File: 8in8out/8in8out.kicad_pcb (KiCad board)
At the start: 2 copper layers, 100.1 x 86.4 mm, 62 parts, among them IC1 ATTINY48-A, J1 RJ45, J2 RJ45, J3 CONN_6, K110 G5T-1-12VDC, K120 G5T-1-12VDC, K130 G5T-1-12VDC, K140 G5T-1-12VDC, K150 G5T-1-12VDC, K160 G5T-1-12VDC, K170 G5T-1-12VDC, K180 G5T-1-12VDC, P1 CONN_5, P100 CONN_2, P101 CONN_2, P102 CONN_2, P103 CONN_2, P105 CONN_2, P106 CONN_2, P110 CONN_2, P120 CONN_2, P130 CONN_2, P140 CONN_2, P150 CONN_2, P160 CONN_2, P170 CONN_2, P180 CONN_2, P2 CONN_5, P3 CONN_10X2, P4 CONN_2, U1 7805, U10 OPTO-TRANSISTOR, U2 ULN2803, U20 OPTO-TRANSISTOR, U30 OPTO-TRANSISTOR, U40 OPTO-TRANSISTOR, U50 OPTO-TRANSISTOR, U60 OPTO-TRANSISTOR, U70 OPTO-TRANSISTOR, U80 OPTO-TRANSISTOR

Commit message: Serigraphie
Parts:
- moved R2 1.78 mm to (269.2, 115.6)
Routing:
- net +12V: track 172.0 -> 173.9 mm
- net N-0000088: track 3.14 -> 4.92 mm
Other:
- board text added: "0 1 2 3"
- board text added: "1"
- board text added: "12V"
- board text added: "12V-GND"
- board text added: "2"
- board text added: "3"
- board text added: "4"
- board text added: "5"
- board text added: "5V"
- board text added: "6"
- board text added: "7"
- board text added: "COM0"
- board text added: "COM1"
- board text added: "FRONT PANEL"
- board text added: "I2C"
- board text added: "I2C PORT"
- board text added: "IN 0"
- board text added: "ISP"
- board text added: "OUT 0"
- board text added: "OUT 1"
- board text added: "OUT 2"
- board text added: "OUT 3"
- board text added: "OUT 4"
- board text added: "OUT 5"
- board text added: "OUT 6"
- board text added: "OUT 7"
- board text added: "STATUS"
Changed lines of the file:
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@@
   (general
     (links 165)
-    (no_connects 14)
+    (no_connects 0)
     (area 180.235859 62.534801 283.060141 169.3672)
     (thickness 1.6002)
-    (drawings 28)
+    (drawings 58)
     (tracks 718)
     (zones 0)
@@
   )
   (layers
-    (15 Dessus signal)
-    (0 Dessous signal)
+    (15 Dessus signal hide)
+    (0 Dessous signal hide)
     (16 B.Adhes user)
     (17 F.Adhes user)
@@
     (23 F.Mask user)
     (24 Dwgs.User user)
-    (25 Cmts.User user)
+    (25 Cmts.User user hide)
     (26 Eco1.User user)
     (27 Eco2.User user)
@@
     (pad_to_mask_clearance 0.254)
     (aux_axis_origin 12.7 12.7)
-    (visible_elements 7FFE7DCF)
+    (visible_elements 7FFF7FFF)
     (pcbplotparams
       (layerselection 15761409)
@@
     (descr "Double rangee de contacts 2 x 12 pins")
     (tags CONN)
-    (fp_text reference P3 (at 0 -3.81) (layer F.SilkS)
+    (fp_text reference P3 (at 1.905 4.064) (layer F.SilkS)
       (effects (font (size 1.016 1.016) (thickness 0.27432)))
     )
@@
     (descr "Connecteurs 2 pins")
     (tags "CONN DEV")
-    (fp_text reference P100 (at 4.318 0.127 90) (layer F.SilkS)
+    (fp_text reference P100 (at 8.128 0.127 90) (layer F.SilkS)
       (effects (font (size 0.762 0.762) (thickness 0.1524)))
     )
@@
     (descr "Connecteurs 2 pins")
     (tags "CONN DEV")
-    (fp_text reference P101 (at 4.318 0.127 90) (layer F.SilkS)
+    (fp_text reference P101 (at 8.128 0.127 90) (layer F.SilkS)
       (effects (font (size 0.762 0.762) (thickness 0.1524)))
     )
@@
     (descr "Connecteurs 2 pins")
     (tags "CONN DEV")
-    (fp_text reference P103 (at 4.318 -0.127 90) (layer F.SilkS)
+    (fp_text reference P103 (at 8.128 -0.127 90) (layer F.SilkS)
       (effects (font (size 0.762 0.762) (thickness 0.1524)))
     )
@@
     (descr "Connecteurs 2 pins")
     (tags "CONN DEV")
-    (fp_text reference P102 (at 4.318 0.127 90) (layer F.SilkS)
+    (fp_text reference P102 (at 8.128 0.127 90) (layer F.SilkS)
       (effects (font (size 0.762 0.762) (thickness 0.1524)))
     )
@@
     (at 215.9 143.51)
     (attr smd)
-    (fp_text reference R51 (at 0 2.032) (layer F.SilkS)
+    (fp_text reference R51 (at 3.556 0 90) (layer F.SilkS)
       (effects (font (size 0.762 0.762) (thickness 0.127)))
     )
@@
   )
   (module SM1206 (layer Dessus)
-    (at 271.018 115.57 270)
+    (at 269.24 115.57 270)
     (attr smd)
     (fp_text reference R2 (at -3.556 0 360) (layer F.SilkS)
@@
     (at 199.39 143.51)
     (attr smd)
-    (fp_text reference R31 (at -1.524 2.286) (layer F.SilkS)
+    (fp_text reference R31 (at 3.556 0 90) (layer F.SilkS)
       (effects (font (size 0.762 0.762) (thickness 0.127)))
     )
@@
     (at 191.135 143.51)
     (attr smd)
-    (fp_text reference R21 (at -0.127 2.286) (layer F.SilkS)
+    (fp_text reference R21 (at 3.429 0 90) (layer F.SilkS)
       (effects (font (size 0.762 0.762) (thickness 0.127)))
     )
@@
     (at 207.518 143.51)
     (attr smd)
-    (fp_text reference R41 (at 0 2.032) (layer F.SilkS)
+    (fp_text reference R41 (at 3.556 0 90) (layer F.SilkS)
       (effects (font (size 0.762 0.762) (thickness 0.127)))
     )
@@
     (at 223.774 143.51)
     (attr smd)
-    (fp_text reference R61 (at 0 2.032) (layer F.SilkS)
+    (fp_text reference R61 (at 0 0 90) (layer F.SilkS)
       (effects (font (size 0.762 0.762) (thickness 0.127)))
     )
@@
     (at 229.235 143.51 180)
     (attr smd)
-    (fp_text reference R71 (at 1.397 -2.032 180) (layer F.SilkS)
+    (fp_text reference R71 (at -1.905 -2.032 180) (layer F.SilkS)
       (effects (font (size 0.762 0.762) (thickness 0.127)))
     )
@@
     (descr "Regulateur TO220 serie LM78xx")
     (tags "TR TO220")
-    (fp_text reference U1 (at -3.175 0 180) (layer F.SilkS)
+    (fp_text reference U1 (at -3.302 -4.318 180) (layer F.SilkS)
       (effects (font (size 1.524 1.016) (thickness 0.2032)))
     )
@@
     )
   )
+  (gr_text 12V-GND (at 241.554 146.304) (layer F.SilkS)
+    (effects (font (size 1.6 1.5) (thickness 0.3)))
+  )
+  (gr_text "I2C PORT" (at 255.27 138.176) (layer F.SilkS)
+    (effects (font (size 1.8 1.5) (thickness 0.3)))
+  )
+  (gr_line (start 226.568 116.84) (end 226.568 117.856) (angle 90) (layer F.SilkS) (width 0.381))
+  (gr_line (start 224.79 116.84) (end 226.568 116.84) (angle 90) (layer F.SilkS) (width 0.381))
+  (gr_line (start 224.79 117.856) (end 224.79 116.84) (angle 90) (layer F.SilkS) (width 0.381))
+  (gr_text ISP (at 226.06 115.062) (layer F.SilkS)
+    (effects (font (size 1.8 1.5) (thickness 0.3)))
+  )
+  (gr_text "FRONT PANEL" (at 207.518 116.332) (layer F.SilkS)
+    (effects (font (size 1.8 1.5) (thickness 0.3)))
+  )
+  (gr_text 12V (at 271.78 115.316 90) (layer F.SilkS)
+    (effects (font (size 1.6 1.5) (thickness 0.3)))
+  )
+  (gr_text 5V (at 279.146 115.51 90) (layer F.SilkS)
+    (effects (font (size 1.6 1.5) (thickness 0.3)))
+  )
+  (gr_text STATUS (at 260.604 114.554 90) (layer F.SilkS)
+    (effects (font (size 1.8 1.5) (thickness 0.3)))
+  )
+  (gr_text I2C (at 257.556 128.27) (layer F.SilkS)
+    (effects (font (size 1.8 1.5) (thickness 0.3)))
+  )
+  (gr_text "0 1 2 3" (at 250.19 122.682) (layer F.SilkS)
+    (effects (font (size 1.8 1.5) (thickness 0.3)))
+  )
+  (gr_text "OUT 7" (at 275.082 83.82) (layer F.SilkS)
+    (effects (font (thickness 0.3048)))
+  )
+  (gr_text "OUT 6" (at 262.89 83.82) (layer F.SilkS)
+    (effects (font (thickness 0.3048)))
+  )
+  (gr_text "OUT 5" (at 250.952 83.82) (layer F.SilkS)
+    (effects (font (thickness 0.3048)))
+  )
+  (gr_text "OUT 4" (at 238.506 83.82) (layer F.SilkS)
+    (effects (font (thickness 0.3048)))
+  )
+  (gr_text "OUT 3" (at 224.282 83.82) (layer F.SilkS)
+    (effects (font (thickness 0.3048)))
+  )
+  (gr_text "OUT 2" (at 212.344 83.82) (layer F.SilkS)
+    (effects (font (thickness 0.3048)))
+  )
+  (gr_text "OUT 1" (at 199.898 83.82) (layer F.SilkS)
+    (effects (font (thickness 0.3048)))
+  )
+  (gr_text "OUT 0" (at 187.96 83.82) (layer F.SilkS)
+    (effects (font (thickness 0.3048)))
+  )
+  (gr_text COM1 (at 224.79 146.558) (layer F.SilkS)
+    (effects (font (thickness 0.3048)))
+  )
+  (gr_text 7 (at 219.71 146.558) (layer F.SilkS)
+    (effects (font (thickness 0.3048)))
+  )
+  (gr_text 6 (at 215.9 146.558) (layer F.SilkS)
+    (effects (font (thickness 0.3048)))
+  )
+  (gr_text 5 (at 212.09 146.558) (layer F.SilkS)
+    (effects (font (thickness 0.3048)))
+  )
+  (gr_text 4 (at 208.28 146.558) (layer F.SilkS)
+    (effects (font (thickness 0.3048)))
+  )
+  (gr_text COM0 (at 202.946 146.558) (layer F.SilkS)
+    (effects (font (thickness 0.3048)))
+  )
+  (gr_text 3 (at 198.12 146.558) (layer F.SilkS)
+    (effects (font (thickness 0.3048)))
+  )
+  (gr_text 2 (at 194.31 146.558) (layer F.SilkS)
+    (effects (font (thickness 0.3048)))
+  )
+  (gr_text 1 (at 190.5 146.558) (layer F.SilkS)
+    (effects (font (thickness 0.3048)))
+  )
+  (gr_text "IN 0" (at 184.912 146.558) (layer F.SilkS)
+    (effects (font (thickness 0.3048)))
+  )
   (gr_line (start 208.661 122.936) (end 208.788 122.936) (angle 90) (layer F.SilkS) (width 0.381))
   (gr_line (start 208.661 124.587) (end 208.661 122.936) (angle 90) (layer F.SilkS) (width 0.381))
@@
   (gr_line (start 281.686 157.48) (end 281.686 71.12) (angle 90) (layer Edge.Cuts) (width 0.381))
   (gr_line (start 181.61 157.48) (end 181.61 71.12) (angle 90) (layer Edge.Cuts) (width 0.381))
+  (segment (start 274.828 110.617) (end 271.145 110.617) (width 0.50038) (layer Dessus) (net 1))
+  (segment (start 269.24 112.522) (end 269.24 113.919) (width 0.50038) (layer Dessus) (net 1))
+  (segment (start 271.145 110.617) (end 269.24 112.522) (width 0.50038) (layer Dessus) (net 1))
   (segment (start 239.649 149.733) (end 239.649 147.701) (width 0.50038) (layer Dessus) (net 1))
   (segment (start 239.649 147.701) (end 245.872 141.478) (width 0.50038) (layer Dessus) (net 1))
@@
   (segment (start 237.49 105.63098) (end 237.49 105.41) (width 0.50038) (layer Dessous) (net 1))
   (segment (start 237.49 105.41) (end 237.49 105.63098) (width 0.50038) (layer Dessous) (net 1))
-  (segment (start 271.018 113.919) (end 271.018 112.776) (width 0.50038) (layer Dessus) (net 1))
-  (segment (start 273.177 110.617) (end 274.828 110.617) (width 0.50038) (layer Dessus) (net 1))
-  (segment (start 271.018 112.776) (end 273.177 110.617) (width 0.50038) (layer Dessus) (net 1))
   (segment (start 255.778 107.823) (end 255.778 108.458) (width 0.50038) (layer Dessous) (net 1))
   (segment (start 255.778 108.458) (end 255.778 110.236) (width 0.50038) (layer Dessous) (net 1))
@@
   (segment (start 189.484 143.51) (end 189.484 139.954) (width 0.254) (layer Dessus) (net 54))
   (segment (start 197.739 143.51) (end 197.739 139.954) (width 0.254) (layer Dessus) (net 55))
-  (segment (start 271.018 117.221) (end 273.83486 117.221) (width 0.254) (layer Dessus) (net 56))
+  (segment (start 269.24 117.221) (end 273.83486 117.221) (width 0.254) (layer Dessus) (net 56))
   (segment (start 273.83486 117.221) (end 274.066 116.98986) (width 0.254) (layer Dessus) (net 56))
   (segment (start 278.384 120.269) (end 278.384 119.02186) (width 0.254) (layer Dessus) (net 57))

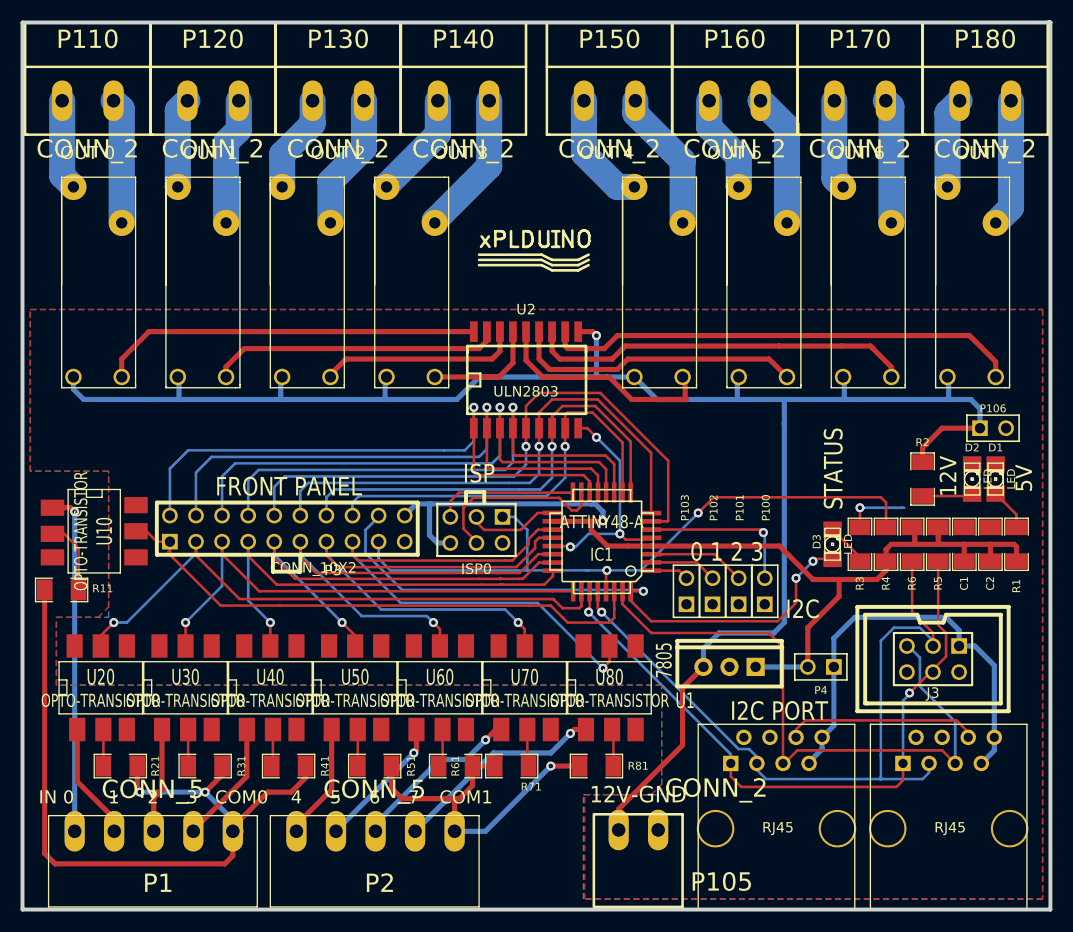
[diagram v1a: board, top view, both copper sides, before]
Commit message: Deplacement optos et r?sistances cause conflit boitier Serigraphie
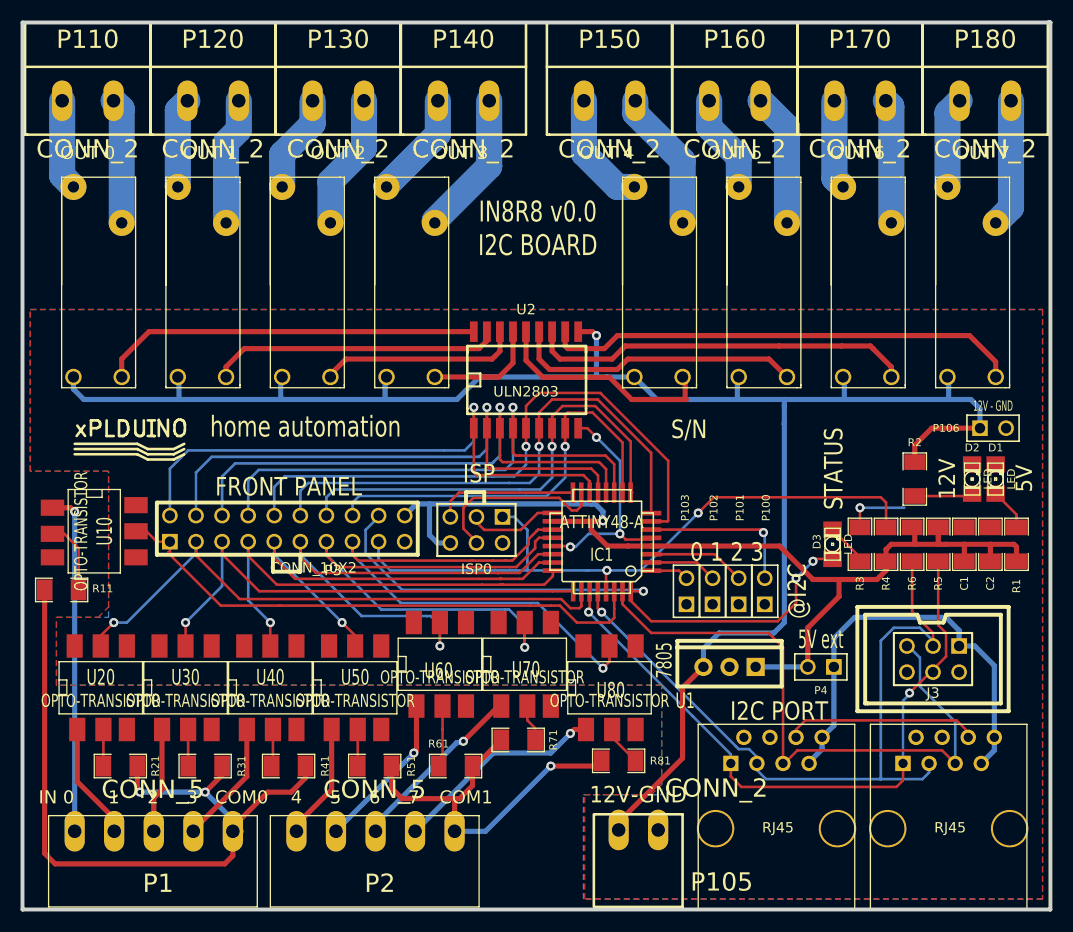
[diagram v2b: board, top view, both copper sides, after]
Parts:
- moved logo_xplduino 43.5 mm to (192.0, 112.4)
- moved R71 2.62 mm to (229.9, 141.0)
- moved U60 2.29 mm to (222.2, 133.6)
- moved U70 2.29 mm to (230.5, 133.6)
- moved R81 2.22 mm to (239.6, 143.0)
- moved R2 0.76 mm to (268.5, 115.6)
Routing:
- net COM1: track 33.4 -> 37.9 mm
- net CMD6: track 50.6 -> 54.3 mm
- net CMD5: track 47.2 -> 50.6 mm
- net IN5: track 13.2 -> 15.6 mm
- net N-0000062: track 3.71 -> 6.00 mm
- net N-0000088: track 4.92 -> 6.01 mm
- net IN6: track 16.8 -> 17.7 mm
- net +12V: track 173.9 -> 174.8 mm
- net N-0000052: track 3.61 -> 4.17 mm
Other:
- board text added: "12V - GND"
- board text added: "5V ext"
- board text added: "@I2C"
- board text added: "IN8R8 v0.0 I2C BOARD"
- board text added: "S/N"
- board text added: "home automation"
- board text removed: "I2C"

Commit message: Final pour prod
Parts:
- added G***: LOGO, OSHWLOGO0.3IN, F.Cu at (227.8, 89.4)
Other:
- board text added: "3 2 1 0 ID 0 0 0 0 0 0 0 0 1 1 0 1 1 0 2 0 1 1 1 3 0 0 0 0 4 0 0 0 1 5 0 1 1 0 6 0 1 1 1 7 1 0 0 0 8 1 0 0 1 9 1 1 1 0 10 1 1 1 1 11 1 0 0 0 12 1 0 0 1 13 1 1 1 0 14 1 1 1 1 15"
- board text added: "@I2C ID TABLE"
- board text removed: "S/N"
